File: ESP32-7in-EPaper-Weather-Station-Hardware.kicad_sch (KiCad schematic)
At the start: 6 parts, among them SW1 SW_Push, U1 DFR0478

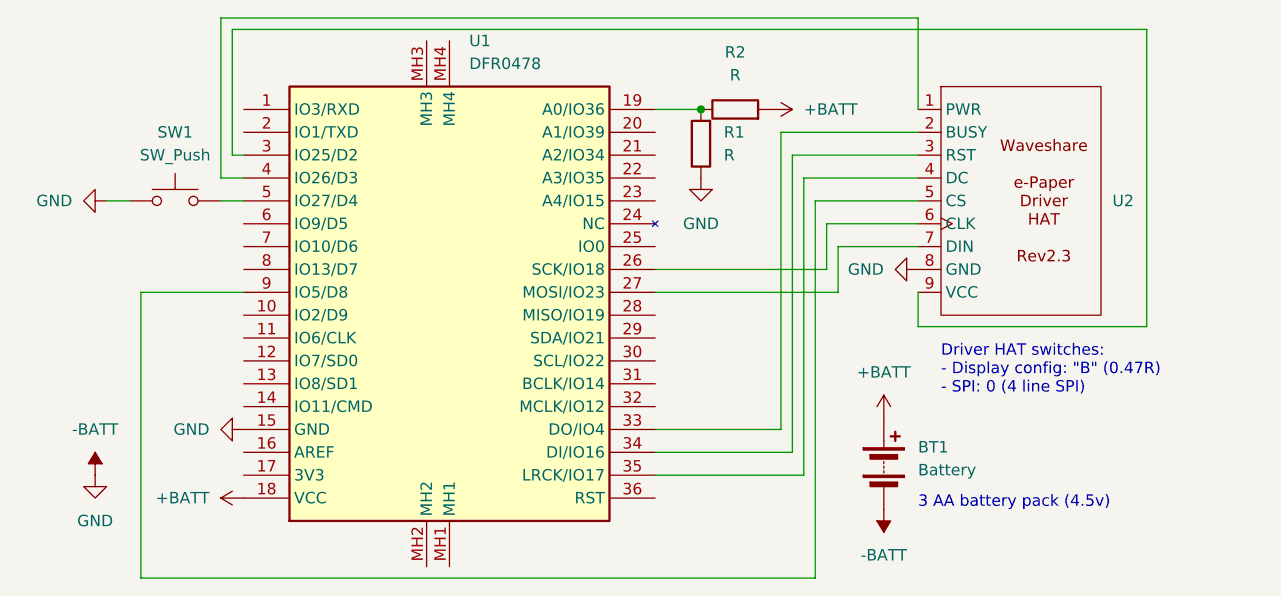
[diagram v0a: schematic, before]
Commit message: Slightly better schematic
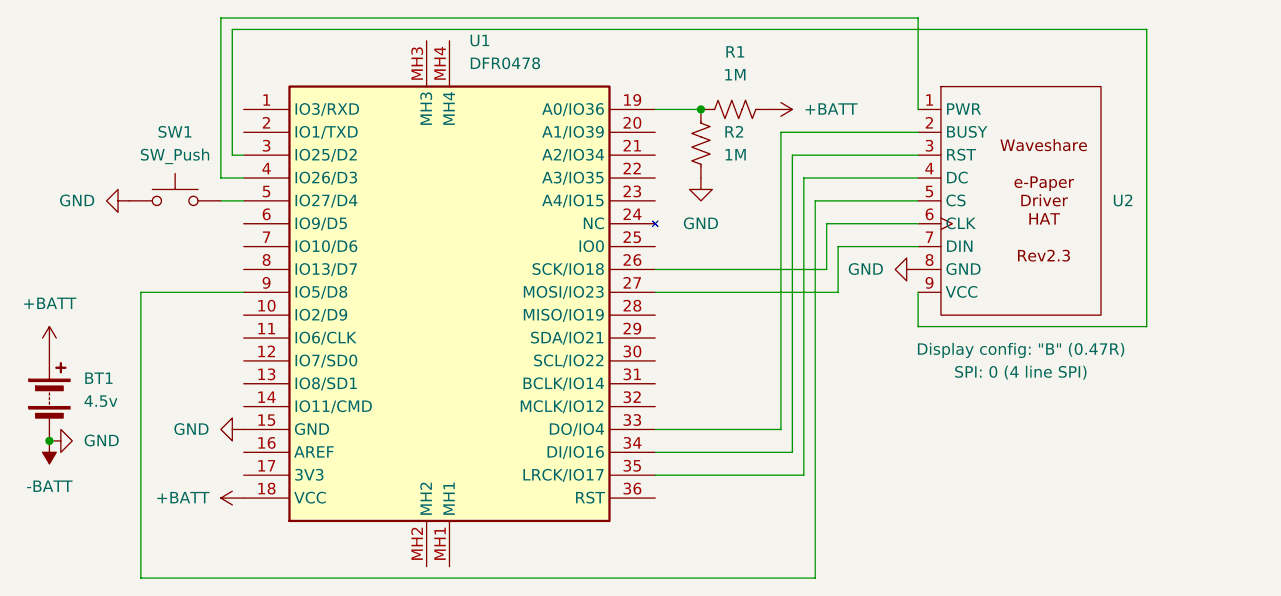
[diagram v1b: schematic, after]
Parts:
- removed R1, R2: R, symbol Device:R
- added R1, R2: 1M, symbol Device:R_US
- BT1: value Battery -> 4.5v
- U2: Display config (none) -> "B" (0.47R); SPI (none) -> 0 (4 line SPI)
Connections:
- net +BATT: now also R1.1
- net -BATT: now also R2.2
- net at U1.19 (A0/IO36): now also R1.2, R2.1
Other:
- note removed: "3 AA battery pack (4.5v)"
- note removed: "Driver HAT switches: - Display config: "B" (0.47R) - SPI: 0 (4 line SPI)"
- moved on the sheet: BT1
